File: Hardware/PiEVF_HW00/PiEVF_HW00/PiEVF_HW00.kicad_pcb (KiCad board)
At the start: 2 copper layers, 65 x 30 mm, 6 parts, among them J1 Conn_02x20_Odd_Even, J2 FR02C061JA1-R5000

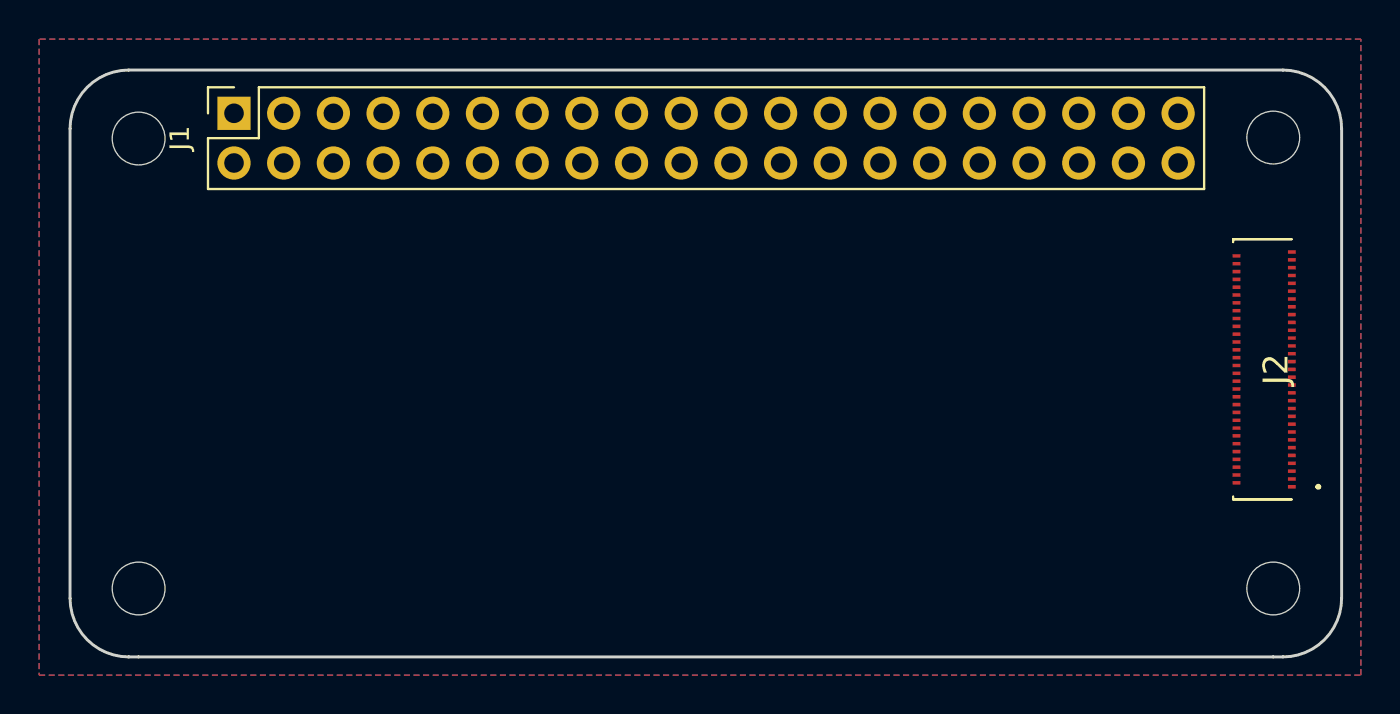
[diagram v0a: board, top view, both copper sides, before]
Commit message: Added RGB to LVDS component
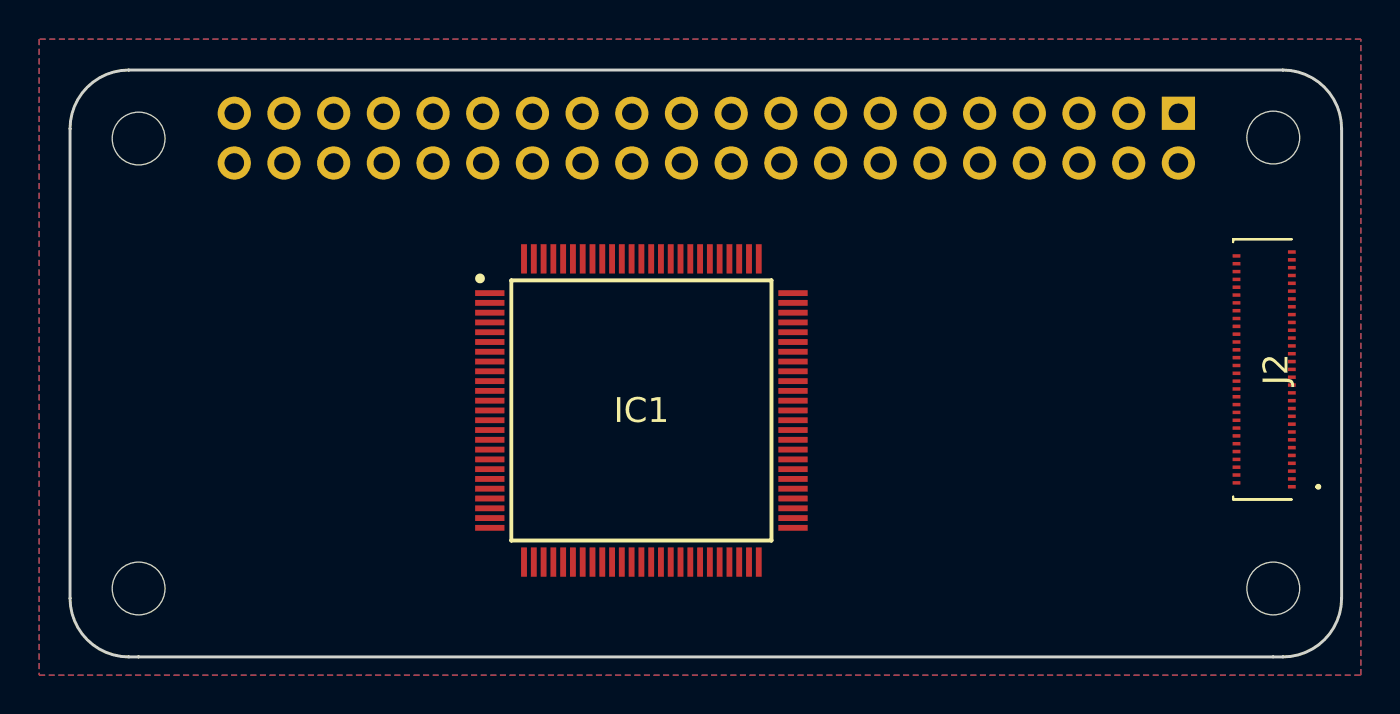
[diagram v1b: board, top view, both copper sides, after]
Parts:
- added IC1: DS90C387VJDX_NOPB, Component_lib:QFP50P1600X1600X120-100N, F.Cu at (127.2, 86.1)
- J1: moved to B.Cu
- moved J1 48.3 mm to (154.7, 70.9)
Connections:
- J2 pad 1: GND -> unconnected-(J2-Pad1)
- J2 pad 10: /VGAM2 -> unconnected-(J2-Pad10)
- J2 pad 11: /VGAM3 -> unconnected-(J2-Pad11)
- J2 pad 12: /VGAM4 -> unconnected-(J2-Pad12)
- J2 pad 13: /VCAL -> unconnected-(J2-Pad13)
- J2 pad 14: GND -> unconnected-(J2-Pad14)
- J2 pad 15: /VDD1 -> unconnected-(J2-Pad15)
- J2 pad 16: /DOUT -> unconnected-(J2-Pad16)
- J2 pad 17: /SO -> unconnected-(J2-Pad17)
- J2 pad 18: /SI -> unconnected-(J2-Pad18)
- J2 pad 19: /XSCK -> unconnected-(J2-Pad19)
- J2 pad 2: /VDD4 -> unconnected-(J2-Pad2)
- J2 pad 20: /XCS -> unconnected-(J2-Pad20)
- J2 pad 21: GND -> unconnected-(J2-Pad21)
- J2 pad 22: /TSTEN -> unconnected-(J2-Pad22)
- J2 pad 23: /SEL_IN -> unconnected-(J2-Pad23)
- J2 pad 24: BLUE0 -> unconnected-(J2-Pad24)
- J2 pad 25: BLUE1 -> unconnected-(J2-Pad25)
- J2 pad 26: BLUE2 -> unconnected-(J2-Pad26)
- J2 pad 27: BLUE3 -> unconnected-(J2-Pad27)
- J2 pad 28: BLUE4 -> unconnected-(J2-Pad28)
- J2 pad 29: BLUE5 -> unconnected-(J2-Pad29)
- J2 pad 3: /DS_HI -> unconnected-(J2-Pad3)
- J2 pad 30: BLUE6 -> unconnected-(J2-Pad30)
- J2 pad 31: BLUE7 -> unconnected-(J2-Pad31)
- J2 pad 32: GND -> unconnected-(J2-Pad32)
- J2 pad 33: /VDD1 -> unconnected-(J2-Pad33)
- J2 pad 34: GREEN0 -> unconnected-(J2-Pad34)
- J2 pad 35: GREEN1 -> unconnected-(J2-Pad35)
- J2 pad 36: GREEN2 -> unconnected-(J2-Pad36)
- J2 pad 37: GREEN3 -> unconnected-(J2-Pad37)
- J2 pad 38: GREEN4 -> unconnected-(J2-Pad38)
- J2 pad 39: GREEN5 -> unconnected-(J2-Pad39)
- J2 pad 4: /VDD2 -> unconnected-(J2-Pad4)
- J2 pad 40: GREEN6 -> unconnected-(J2-Pad40)
- J2 pad 41: GREEN7 -> unconnected-(J2-Pad41)
- J2 pad 42: RED0 -> unconnected-(J2-Pad42)
- J2 pad 43: RED1 -> unconnected-(J2-Pad43)
- J2 pad 44: RED2 -> unconnected-(J2-Pad44)
- J2 pad 45: RED3 -> unconnected-(J2-Pad45)
- J2 pad 46: RED4 -> unconnected-(J2-Pad46)
- J2 pad 47: RED5 -> unconnected-(J2-Pad47)
- J2 pad 48: RED6 -> unconnected-(J2-Pad48)
- J2 pad 49: RED7 -> unconnected-(J2-Pad49)
- J2 pad 5: /VDD3 -> unconnected-(J2-Pad5)
- J2 pad 50: /XCLR -> unconnected-(J2-Pad50)
- J2 pad 51: V-SYNC -> unconnected-(J2-Pad51)
- J2 pad 52: H-SYNC -> unconnected-(J2-Pad52)
- J2 pad 53: CLK -> unconnected-(J2-Pad53)
- J2 pad 54: /VDD1 -> unconnected-(J2-Pad54)
- J2 pad 55: GND -> unconnected-(J2-Pad55)
- J2 pad 56: GND -> unconnected-(J2-Pad56)
- J2 pad 57: /VDD3 -> unconnected-(J2-Pad57)
- J2 pad 58: /VDD2 -> unconnected-(J2-Pad58)
- J2 pad 59: /DS_HI -> unconnected-(J2-Pad59)
- J2 pad 6: GND -> unconnected-(J2-Pad6)
- J2 pad 60: /VDD4 -> unconnected-(J2-Pad60)
- J2 pad 61: GND -> unconnected-(J2-Pad61)
- J2 pad 7: GND -> unconnected-(J2-Pad7)
- J2 pad 8: /VGAM0 -> unconnected-(J2-Pad8)
- J2 pad 9: /VGAM1 -> unconnected-(J2-Pad9)
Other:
- copper layers 2 -> 4

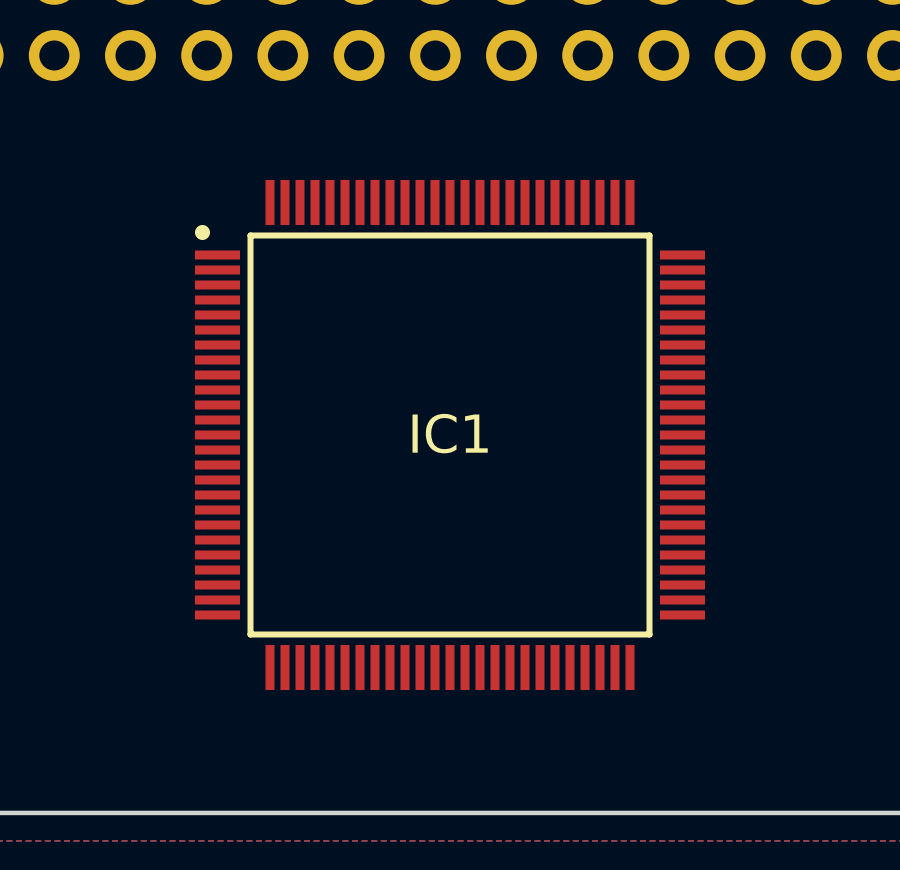
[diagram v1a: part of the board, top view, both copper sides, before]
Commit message: removed lvds chip
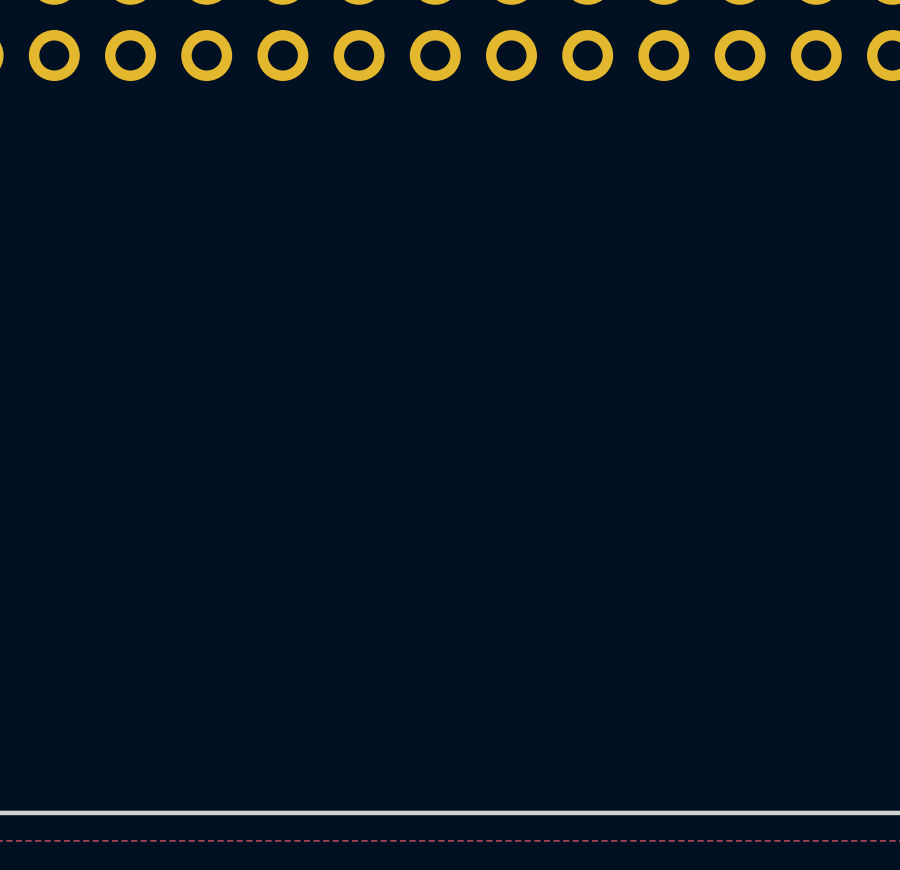
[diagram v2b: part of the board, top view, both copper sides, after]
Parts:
- removed IC1: DS90C387VJDX_NOPB, Component_lib:QFP50P1600X1600X120-100N

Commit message: hold on, it may be lvds
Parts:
- added IC1: DS90C387VJDX_NOPB, Component_lib:QFP50P1600X1600X120-100N, F.Cu at (131.9, 86.2)
